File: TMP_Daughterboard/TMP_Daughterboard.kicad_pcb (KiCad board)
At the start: 2 copper layers, 1 part, among them U1 TMP1075NDRLR

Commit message: daughter tmp board
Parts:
- U1: footprint TMP_Daughterboard:TMP1075-MOD-A -> TMP_Daughterboard:TMP1075-MOD-B
- moved U1 2.85 mm to (152.4, 101.6)
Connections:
- U1 pad 2: unconnected-(U1-GND-Pad2) -> Net-(U1-A0)
- U1 pad 4: unconnected-(U1-A0-Pad4) -> Net-(U1-A0)
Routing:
- net Net-(U1-A0): track 0.00 -> 3.27 mm
- net unconnected-(U1-SDA-Pad6): track 0.00 -> 1.01 mm
- net unconnected-(U1-V+-Pad5): track 0.00 -> 1.00 mm
- net unconnected-(U1-ALERT-Pad3): track 0.00 -> 0.98 mm
- net unconnected-(U1-SCL-Pad1): track 0.00 -> 0.94 mm
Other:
- board outline added: 4.6 x 5.2 mm

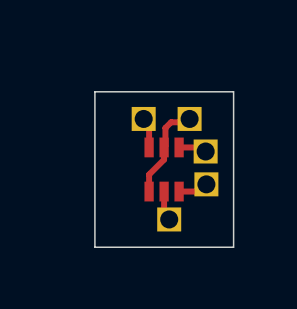
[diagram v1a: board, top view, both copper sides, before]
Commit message: daughter tmp board outline
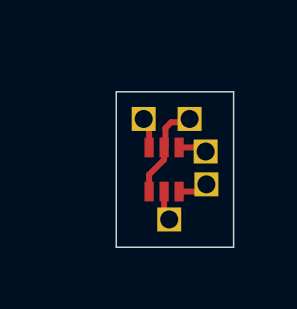
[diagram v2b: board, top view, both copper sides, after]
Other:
- board size 4.6 x 5.2 mm -> 3.9 x 5.2 mm
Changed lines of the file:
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@@
 		(capping no)
 		(filling no)
-		(zone_defaults)
 		(pcbplotparams
 			(layerselection 0x00000000_00000000_55555555_5755f5ff)
@@
 		(sheetname "/")
 		(sheetfile "TMP_Daughterboard.kicad_sch")
-		(solder_mask_margin 0)
-		(clearance 0.1)
+		(clearance 0.19)
 		(attr smd)
 		(duplicate_pad_numbers_are_jumpers no)
@@
 			(pinfunction "SCL_1")
 			(pintype "input")
-			(solder_mask_margin 0.102)
+			(solder_mask_margin 0.08)
 		)
 		(pad "1" thru_hole rect
@@
 			(pinfunction "GND_2")
 			(pintype "passive")
-			(solder_mask_margin 0.102)
+			(solder_mask_margin 0.08)
 		)
 		(pad "2" thru_hole rect
@@
 			(pinfunction "ALERT_3")
 			(pintype "output")
-			(solder_mask_margin 0.102)
+			(solder_mask_margin 0.08)
 		)
 		(pad "4" smd rect
@@
 			(pinfunction "A0_4")
 			(pintype "passive")
-			(solder_mask_margin 0.102)
+			(solder_mask_margin 0.08)
 		)
 		(pad "5" smd rect
-			(at 0.02 0.785 270)
+			(at 0.02 0.785 90)
 			(size 0.66 0.31)
 			(layers "F.Cu" "F.Mask" "F.Paste")
@@
 			(pinfunction "V+_5")
 			(pintype "power_in")
-			(solder_mask_margin 0.102)
+			(solder_mask_margin 0.08)
 		)
 		(pad "5" thru_hole rect
@@
 			(pinfunction "SDA_6")
 			(pintype "bidirectional")
-			(solder_mask_margin 0.102)
+			(solder_mask_margin 0.08)
 		)
 		(pad "6" thru_hole rect
@@
 	)
 	(gr_rect
-		(start 150.114 99.06)
+		(start 150.8252 99.06)
 		(end 154.7368 104.2416)
 		(stroke
@@
 	)
 	(segment
+		(start 153.67 100.915)
+		(end 153.805 101.05)
+		(width 0.2)
+		(layer "F.Cu")
+		(net "unconnected-(U1-SCL-Pad1)")
+	)
+	(segment
+		(start 152.92 100.915)
+		(end 153.67 100.915)
+		(width 0.2)
+		(layer "F.Cu")
+		(net "unconnected-(U1-SCL-Pad1)")
+	)
+	(segment
+		(start 153.159165 100.076)
+		(end 152.654 100.076)
+		(width 0.2)
+		(layer "F.Cu")
+		(net "Net-(U1-A0)")
+	)
+	(segment
+		(start 152.465 100.87)
+		(end 152.42 100.915)
+		(width 0.2)
+		(layer "F.Cu")
+		(net "Net-(U1-A0)")
+	)
+	(segment
+		(start 152.465 100.265)
+		(end 152.465 100.87)
+		(width 0.2)
+		(layer "F.Cu")
+		(net "Net-(U1-A0)")
+	)
+	(segment
+		(start 152.654 100.076)
+		(end 152.465 100.265)
+		(width 0.2)
+		(layer "F.Cu")
+		(net "Net-(U1-A0)")
+	)
+	(segment
+		(start 153.27 99.965165)
+		(end 153.159165 100.076)
+		(width 0.2)
+		(layer "F.Cu")
+		(net "Net-(U1-A0)")
+	)
+	(segment
+		(start 151.92 101.82)
+		(end 151.92 102.385)
+		(width 0.2)
+		(layer "F.Cu")
+		(net "Net-(U1-A0)")
+	)
+	(segment
+		(start 152.42 100.915)
+		(end 152.42 101.32)
+		(width 0.2)
+		(layer "F.Cu")
+		(net "Net-(U1-A0)")
+	)
+	(segment
+		(start 152.42 101.32)
+		(end 151.92 101.82)
+		(width 0.2)
+		(layer "F.Cu")
+		(net "Net-(U1-A0)")
+	)
+	(segment
+		(start 151.92 100.040165)
+		(end 151.845 99.965165)
+		(width 0.2)
+		(layer "F.Cu")
+		(net "unconnected-(U1-ALERT-Pad3)")
+	)
+	(segment
+		(start 151.92 100.915)
+		(end 151.92 100.040165)
+		(width 0.2)
+		(layer "F.Cu")
+		(net "unconnected-(U1-ALERT-Pad3)")
+	)
+	(segment
 		(start 152.42 103.145165)
 		(end 152.59 103.315165)
@@
 	)
 	(segment
-		(start 151.92 100.040165)
-		(end 151.845 99.965165)
-		(width 0.2)
-		(layer "F.Cu")
-		(net "unconnected-(U1-ALERT-Pad3)")
-	)
-	(segment
-		(start 151.92 100.915)
-		(end 151.92 100.040165)
-		(width 0.2)
-		(layer "F.Cu")
-		(net "unconnected-(U1-ALERT-Pad3)")
-	)
-	(segment
-		(start 153.159165 100.076)
-		(end 152.654 100.076)
-		(width 0.2)
-		(layer "F.Cu")
-		(net "Net-(U1-A0)")
-	)
-	(segment
-		(start 152.465 100.87)
-		(end 152.42 100.915)
-		(width 0.2)
-		(layer "F.Cu")
-		(net "Net-(U1-A0)")
-	)
-	(segment
-		(start 152.465 100.265)
-		(end 152.465 100.87)
-		(width 0.2)
-		(layer "F.Cu")
-		(net "Net-(U1-A0)")
-	)
-	(segment
-		(start 152.654 100.076)
-		(end 152.465 100.265)
-		(width 0.2)
-		(layer "F.Cu")
-		(net "Net-(U1-A0)")
-	)
-	(segment
-		(start 153.27 99.965165)
-		(end 153.159165 100.076)
-		(width 0.2)
-		(layer "F.Cu")
-		(net "Net-(U1-A0)")
-	)
-	(segment
-		(start 151.92 101.82)
-		(end 151.92 102.385)
-		(width 0.2)
-		(layer "F.Cu")
-		(net "Net-(U1-A0)")
-	)
-	(segment
-		(start 152.42 100.915)
-		(end 152.42 101.32)
-		(width 0.2)
-		(layer "F.Cu")
-		(net "Net-(U1-A0)")
-	)
-	(segment
-		(start 152.42 101.32)
-		(end 151.92 101.82)
-		(width 0.2)
-		(layer "F.Cu")
-		(net "Net-(U1-A0)")
-	)
-	(segment
-		(start 153.67 100.915)
-		(end 153.805 101.05)
-		(width 0.2)
-		(layer "F.Cu")
-		(net "unconnected-(U1-SCL-Pad1)")
-	)
-	(segment
-		(start 152.92 100.915)
-		(end 153.67 100.915)
-		(width 0.2)
-		(layer "F.Cu")
-		(net "unconnected-(U1-SCL-Pad1)")
-	)
-	(segment

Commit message: rounded corners for the TMP PCB
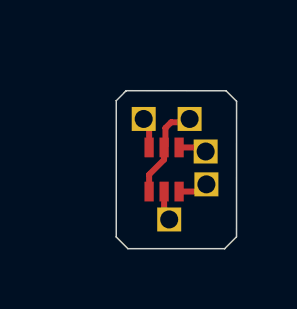
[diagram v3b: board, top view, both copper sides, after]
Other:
- board size 3.9 x 5.2 mm -> 4 x 5.3 mm
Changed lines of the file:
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@@
 		(embedded_fonts no)
 	)
-	(gr_rect
-		(start 150.8252 99.06)
-		(end 154.7368 104.2416)
+	(gr_poly
+		(pts
+			(xy 150.8252 99.355023) (xy 151.155747 99.024027) (xy 154.4863 99.026086) (xy 154.836014 99.376232)
+			(xy 154.833998 103.895523) (xy 154.439433 104.289645) (xy 151.214809 104.289616) (xy 150.8252 103.9)
+		)
 		(stroke
 			(width 0.05)
-			(type default)
+			(type solid)
 		)
 		(fill no)
